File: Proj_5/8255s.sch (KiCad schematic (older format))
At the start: 18 parts, among them J1 Conn_02x15_Top_Bottom, J2 Conn_02x15_Top_Bottom, J3 Conn_02x15_Top_Bottom, U1 8255, U2 8255, U3 8255, U39 74LVC1G11, U40 74LVC1G11, U41 74AHC1G08, U42 74LVC1G11, U43 74AHC1G08, U44 74LVC1G11, U45 74AHC1G08, U46 74LVC1G11, U47 PAL16L8

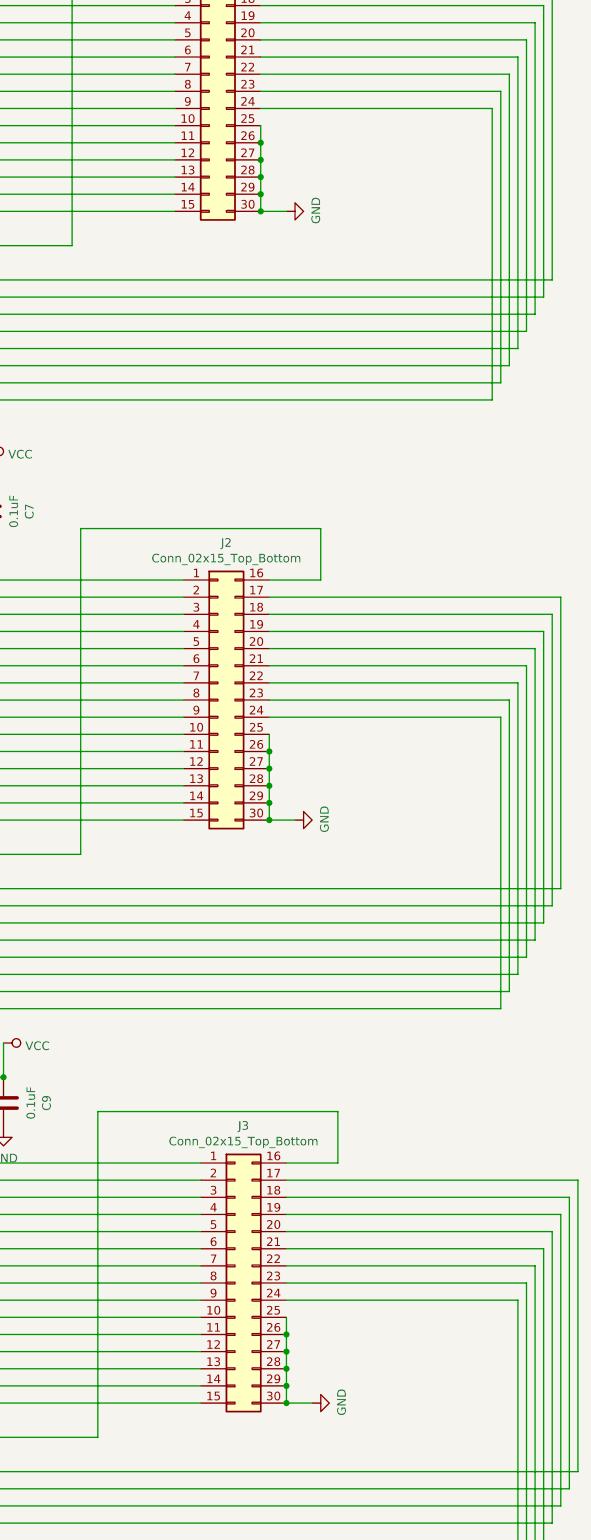
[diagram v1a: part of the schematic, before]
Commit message: Added at least 4 Footprints
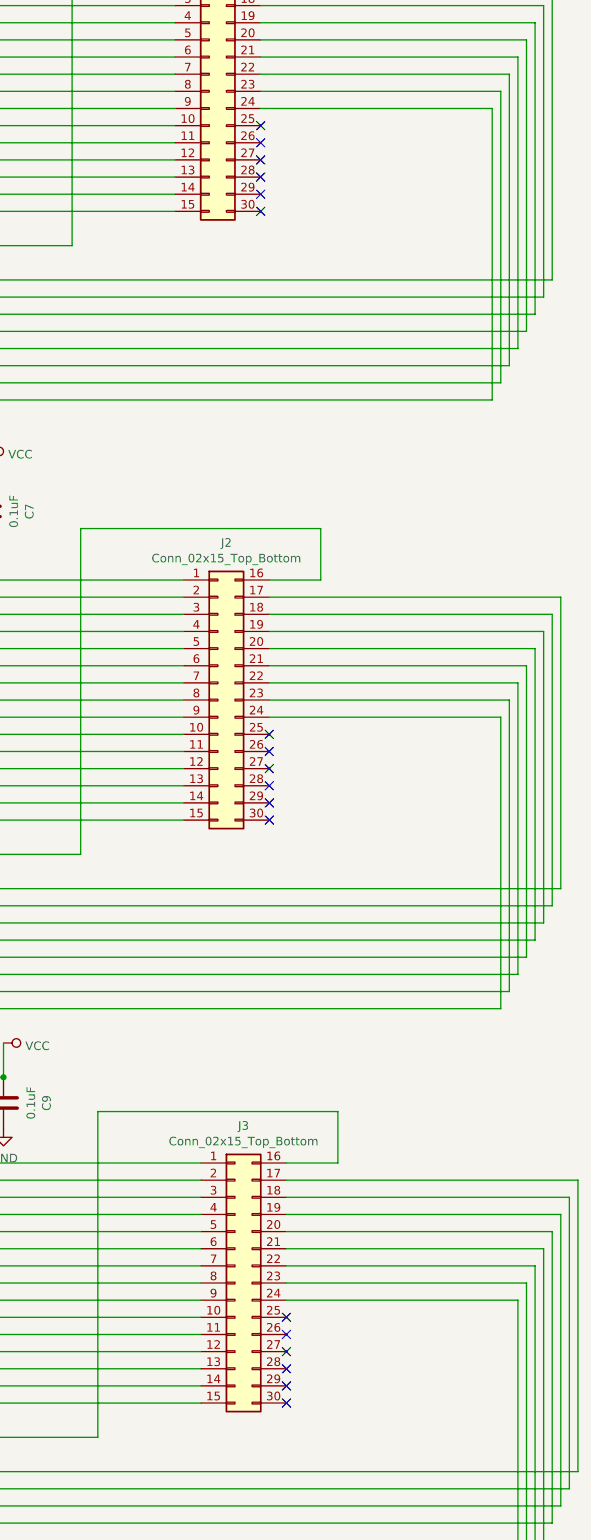
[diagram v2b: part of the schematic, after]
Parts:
- C7, C8, C9: footprint (none) -> Capacitor_Tantalum_SMD:CP_EIA-1608-08_AVX-J
- J1, J2, J3: footprint (none) -> Connector_PinHeader_1.00mm:PinHeader_2x15_P1.00mm_Vertical
- U47: footprint (none) -> Package_DIP:DIP-20_W7.62mm
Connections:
- net GND: no longer J1.25 (Pin_25), J1.26 (Pin_26), J1.27 (Pin_27), J1.28 (Pin_28), J1.29 (Pin_29), J1.30 (Pin_30), J2.25 (Pin_25), J2.26 (Pin_26), J2.27 (Pin_27), J2.28 (Pin_28), J2.29 (Pin_29), J2.30 (Pin_30), J3.25 (Pin_25), J3.26 (Pin_26), J3.27 (Pin_27), J3.28 (Pin_28), J3.29 (Pin_29), J3.30 (Pin_30)
- no-connect marks 10 -> 28
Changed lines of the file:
@@
 F 0 "U47" H 3650 5381 50  0000 C CNN
 F 1 "PAL16L8" H 3650 5290 50  0000 C CNN
-F 2 "" H 3650 4500 50  0001 C CNN
+F 2 "Package_DIP:DIP-20_W7.62mm" H 3650 4500 50  0001 C CNN
 F 3 "" H 3650 4500 50  0001 C CNN
 	1    3650 4500
@@
 F 0 "J2" H 11700 6467 50  0000 C CNN
 F 1 "Conn_02x15_Top_Bottom" H 11700 6376 50  0000 C CNN
-F 2 "" H 11650 5550 50  0001 C CNN
+F 2 "Connector_PinHeader_1.00mm:PinHeader_2x15_P1.00mm_Vertical" H 11650 5550 50  0001 C CNN
 F 3 "~" H 11650 5550 50  0001 C CNN
 	1    11650 5550
@@
 	13300 5650 11950 5650
 Wire Wire Line
-	11950 5750 11950 5850
-Connection ~ 11950 5850
-Wire Wire Line
-	11950 5850 11950 5950
-Connection ~ 11950 5950
-Wire Wire Line
-	11950 5950 11950 6050
-Connection ~ 11950 6050
-Wire Wire Line
-	11950 6050 11950 6150
-Connection ~ 11950 6150
-Wire Wire Line
-	11950 6150 11950 6250
-Wire Wire Line
-	11950 6250 12100 6250
-Connection ~ 11950 6250
-$Comp
-L power:GND #PWR?
-U 1 1 5F836F32
-P 12100 6250
-AR Path="/5EA993EC/5F836F32" Ref="#PWR?"  Part="1"
-AR Path="/5EA0416B/5F836F32" Ref="#PWR060"  Part="1"
-F 0 "#PWR060" H 12100 6000 50  0001 C CNN
-F 1 "GND" H 12105 6077 50  0000 C CNN
-F 2 "" H 12100 6250 50  0001 C CNN
-F 3 "" H 12100 6250 50  0001 C CNN
-	1    12100 6250
-	0    -1   -1   0
-$EndComp
-Wire Wire Line
 	9750 5750 9850 5750
 Wire Wire Line
@@
 F 0 "J1" H 11650 2917 50  0000 C CNN
 F 1 "Conn_02x15_Top_Bottom" H 11650 2826 50  0000 C CNN
-F 2 "" H 11600 2000 50  0001 C CNN
+F 2 "Connector_PinHeader_1.00mm:PinHeader_2x15_P1.00mm_Vertical" H 11600 2000 50  0001 C CNN
 F 3 "~" H 11600 2000 50  0001 C CNN
 	1    11600 2000
@@
 Wire Wire Line
 	13250 2100 11900 2100
-Wire Wire Line
-	11900 2200 11900 2300
-Connection ~ 11900 2300
-Wire Wire Line
-	11900 2300 11900 2400
-Connection ~ 11900 2400
-Wire Wire Line
-	11900 2400 11900 2500
-Connection ~ 11900 2500
-Wire Wire Line
-	11900 2500 11900 2600
-Connection ~ 11900 2600
-Wire Wire Line
-	11900 2600 11900 2700
-Wire Wire Line
-	11900 2700 12050 2700
-Connection ~ 11900 2700
-$Comp
-L power:GND #PWR?
-U 1 1 5F942863
-P 12050 2700
-AR Path="/5EA993EC/5F942863" Ref="#PWR?"  Part="1"
-AR Path="/5EA0416B/5F942863" Ref="#PWR059"  Part="1"
-F 0 "#PWR059" H 12050 2450 50  0001 C CNN
-F 1 "GND" H 12055 2527 50  0000 C CNN
-F 2 "" H 12050 2700 50  0001 C CNN
-F 3 "" H 12050 2700 50  0001 C CNN
-	1    12050 2700
-	0    -1   -1   0
-$EndComp
 Wire Wire Line
 	9700 2200 9800 2200
@@
 F 0 "J3" H 11800 9867 50  0000 C CNN
 F 1 "Conn_02x15_Top_Bottom" H 11800 9776 50  0000 C CNN
-F 2 "" H 11750 8950 50  0001 C CNN
+F 2 "Connector_PinHeader_1.00mm:PinHeader_2x15_P1.00mm_Vertical" H 11750 8950 50  0001 C CNN
 F 3 "~" H 11750 8950 50  0001 C CNN
 	1    11750 8950
@@
 Wire Wire Line
 	13400 9050 12050 9050
-Wire Wire Line
-	12050 9150 12050 9250
-Connection ~ 12050 9250
-Wire Wire Line
-	12050 9250 12050 9350
-Connection ~ 12050 9350
-Wire Wire Line
-	12050 9350 12050 9450
-Connection ~ 12050 9450
-Wire Wire Line
-	12050 9450 12050 9550
-Connection ~ 12050 9550
-Wire Wire Line
-	12050 9550 12050 9650
-Wire Wire Line
-	12050 9650 12200 9650
-Connection ~ 12050 9650
-$Comp
-L power:GND #PWR?
-U 1 1 5F955658
-P 12200 9650
-AR Path="/5EA993EC/5F955658" Ref="#PWR?"  Part="1"
-AR Path="/5EA0416B/5F955658" Ref="#PWR061"  Part="1"
-F 0 "#PWR061" H 12200 9400 50  0001 C CNN
-F 1 "GND" H 12205 9477 50  0000 C CNN
-F 2 "" H 12200 9650 50  0001 C CNN
-F 3 "" H 12200 9650 50  0001 C CNN
-	1    12200 9650
-	0    -1   -1   0
-$EndComp
 Wire Wire Line
 	9850 9150 9950 9150
@@
 F 0 "C9" V 10148 7900 50  0000 C CNN
 F 1 "0.1uF" V 10239 7900 50  0000 C CNN
-F 2 "" H 10438 7750 50  0001 C CNN
+F 2 "Capacitor_Tantalum_SMD:CP_EIA-1608-08_AVX-J" H 10438 7750 50  0001 C CNN
 F 3 "~" H 10400 7900 50  0001 C CNN
 	1    10400 7900
@@
 F 0 "C7" V 10048 4450 50  0000 C CNN
 F 1 "0.1uF" V 10139 4450 50  0000 C CNN
-F 2 "" H 10338 4300 50  0001 C CNN
+F 2 "Capacitor_Tantalum_SMD:CP_EIA-1608-08_AVX-J" H 10338 4300 50  0001 C CNN
 F 3 "~" H 10300 4450 50  0001 C CNN
 	1    10300 4450
@@
 F 0 "C8" V 10148 950 50  0000 C CNN
 F 1 "0.1uF" V 10239 950 50  0000 C CNN
-F 2 "" H 10438 800 50  0001 C CNN
+F 2 "Capacitor_Tantalum_SMD:CP_EIA-1608-08_AVX-J" H 10438 800 50  0001 C CNN
 F 3 "~" H 10400 950 50  0001 C CNN
 	1    10400 950
@@
 	8650 4200 9000 4200
 Connection ~ 8050 8700
+NoConn ~ 11950 5750
+NoConn ~ 11950 5850
+NoConn ~ 11950 5950
+NoConn ~ 11950 6050
+NoConn ~ 11950 6150
+NoConn ~ 11950 6250
+NoConn ~ 12050 9150
+NoConn ~ 12050 9250
+NoConn ~ 12050 9350
+NoConn ~ 12050 9450
+NoConn ~ 12050 9550
+NoConn ~ 12050 9650
+NoConn ~ 11900 2700
+NoConn ~ 11900 2600
+NoConn ~ 11900 2500
+NoConn ~ 11900 2400
+NoConn ~ 11900 2300
+NoConn ~ 11900 2200
 Wire Bus Line
 	5200 8700 8050 8700

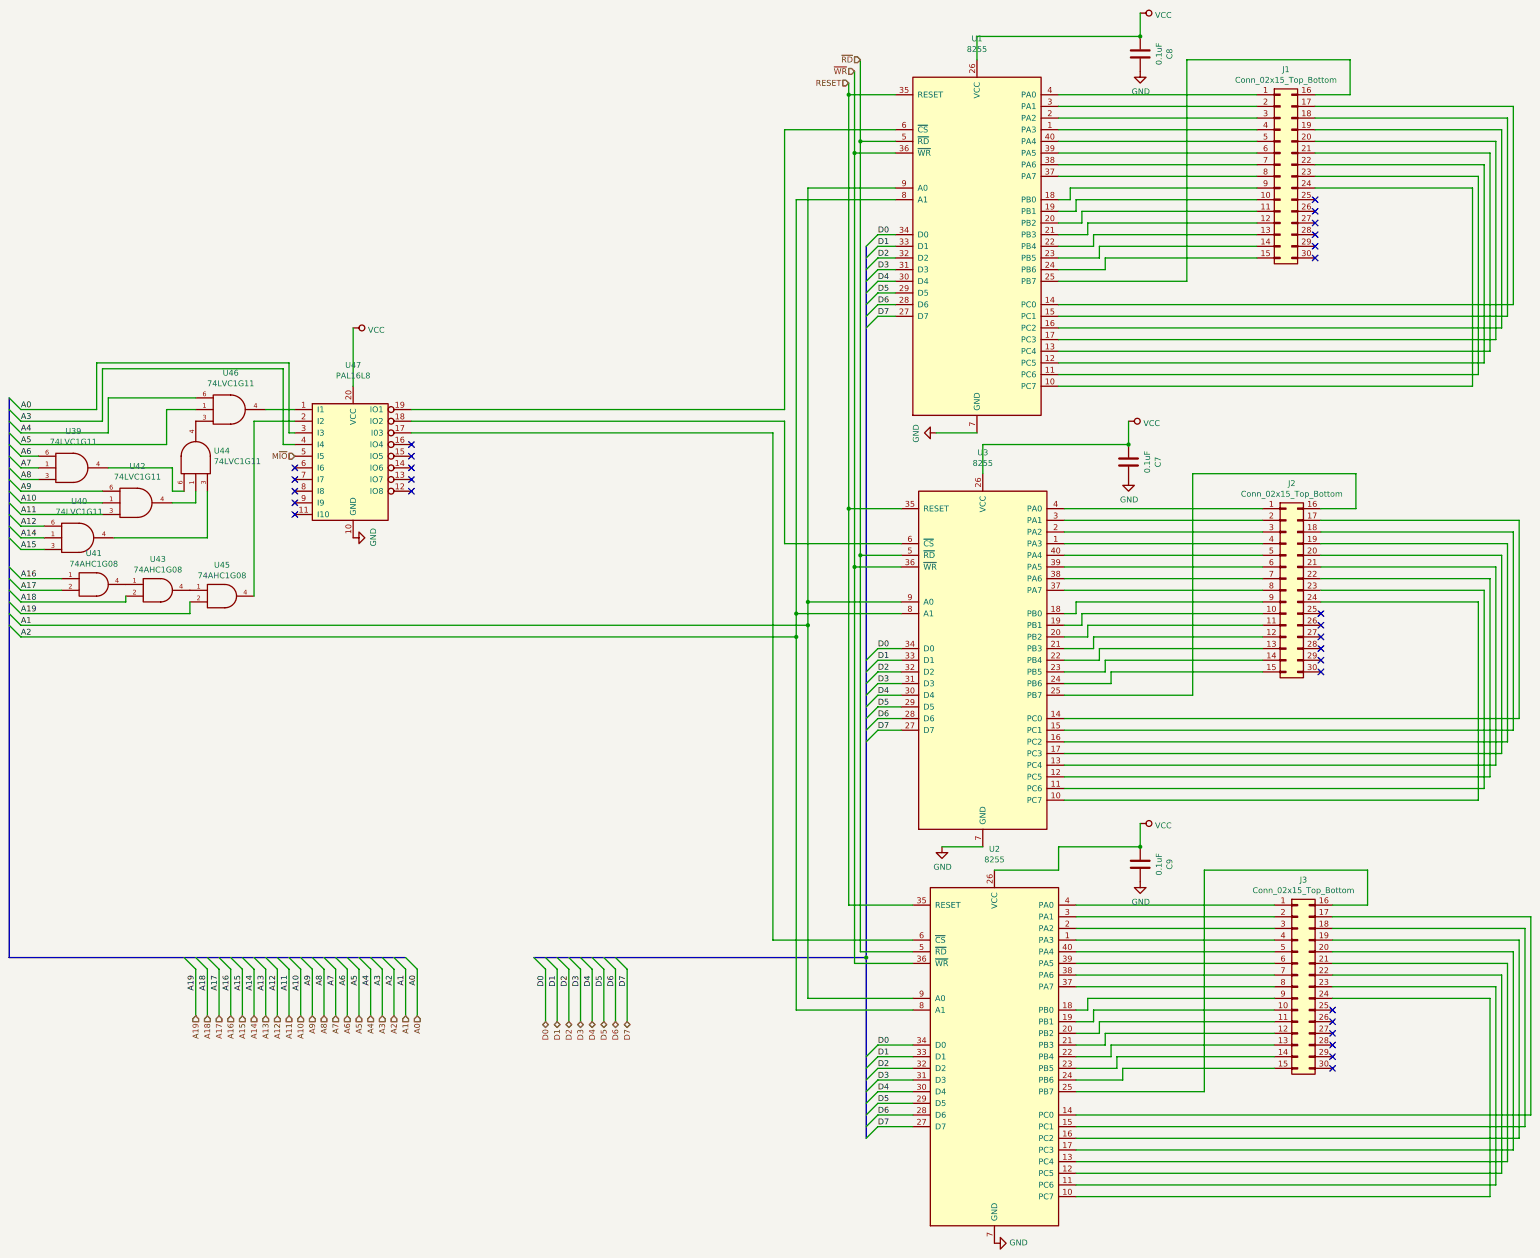
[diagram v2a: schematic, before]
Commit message: No more and gates
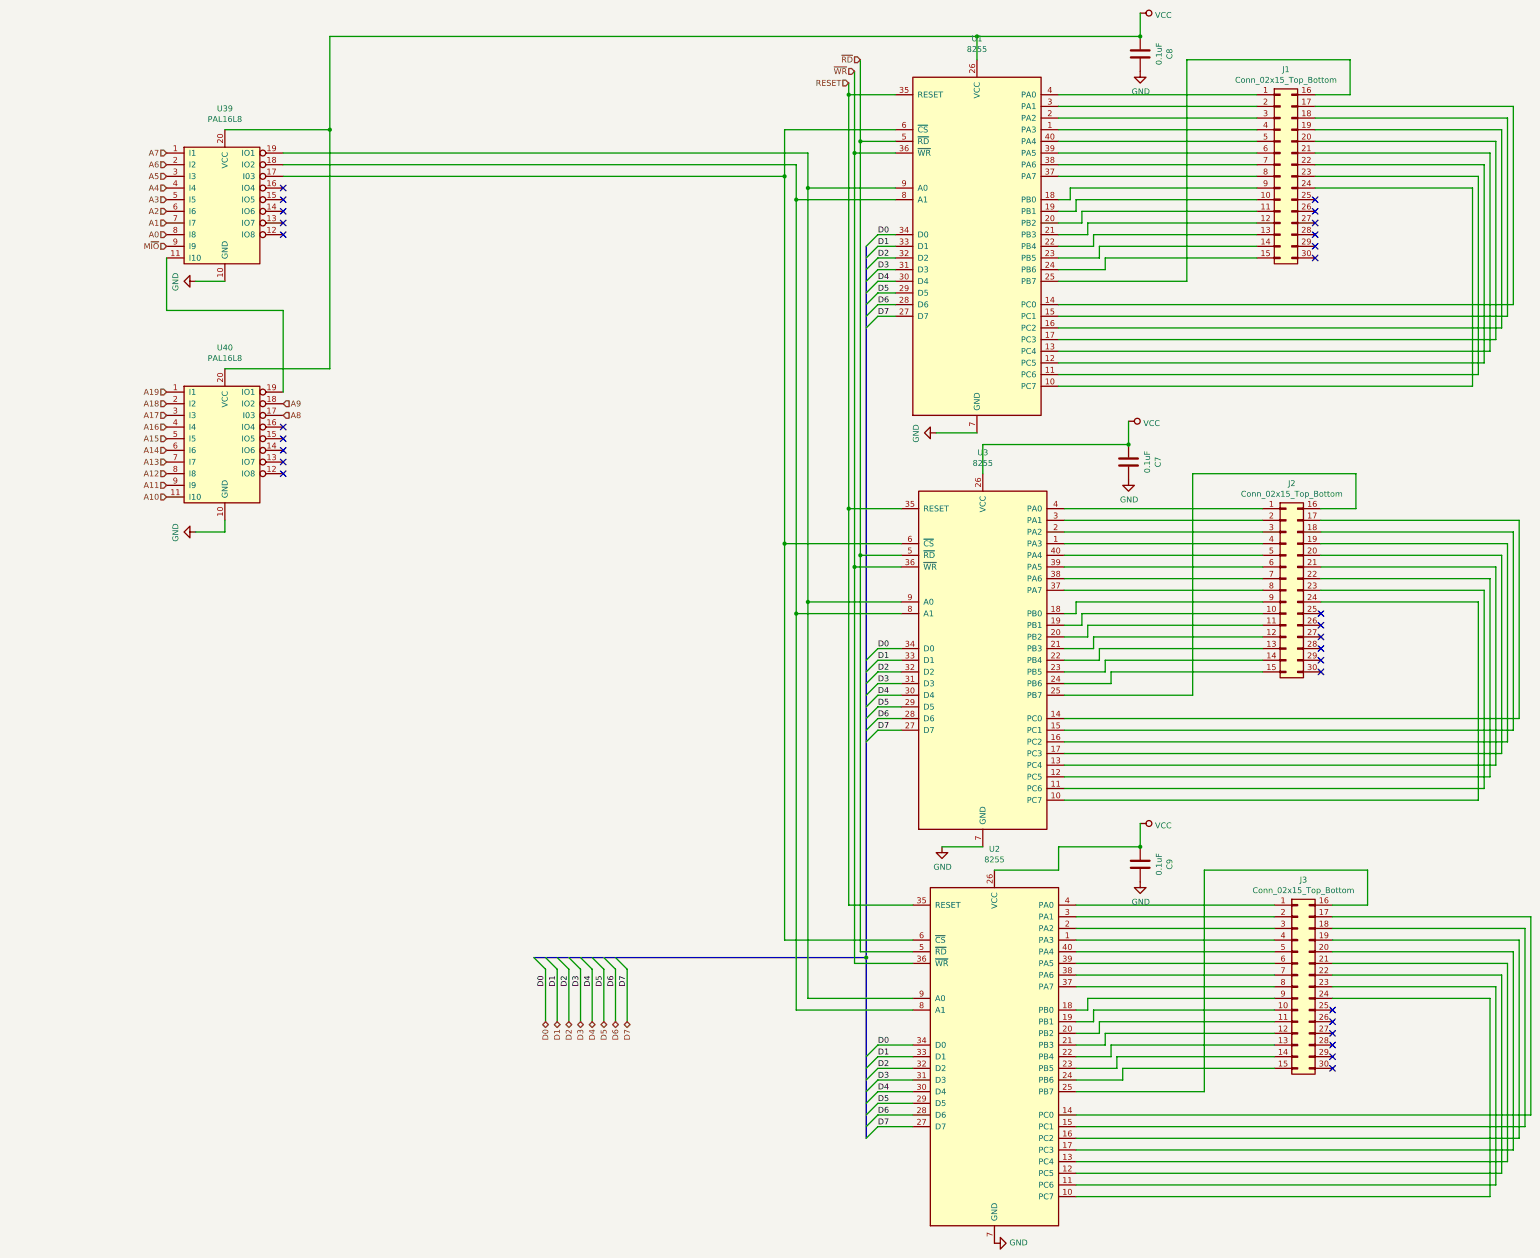
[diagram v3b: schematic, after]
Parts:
- removed U39, U40, U42, U44, U46: 74LVC1G11, symbol 74xGxx:74LVC1G11
- removed U41, U43, U45: 74AHC1G08, symbol 74xGxx:74AHC1G08
- removed U47: PAL16L8, Package_DIP:DIP-20_W7.62mm, symbol Logic_Programmable:PAL16L8
- added U39, U40: PAL16L8, Package_DIP:DIP-20_W7.62mm, symbol Logic_Programmable:PAL16L8
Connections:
- net A0: now also U39.8 (I8)
- net A1: now also U39.7 (I7); no longer U1.9 (A0), U2.9 (A0), U3.9 (A0)
- net A10: now also U40.11 (I10)
- net A11: now also U40.9 (I9)
- net A12: now also U40.8 (I8)
- net A13: now also U40.7 (I7)
- net A14: now also U40.6 (I6)
- net A15: now also U40.5 (I5)
- net A16: now also U40.4 (I4)
- net A17: now also U40.3 (I3)
- net A18: now also U40.2 (I2)
- net A19: now also U40.1 (I1)
- net A2: now also U39.6 (I6); no longer U1.8 (A1), U2.8 (A1), U3.8 (A1)
- net A3: now also U39.5 (I5)
- net A4: now also U39.4 (I4)
- net A5: now also U39.3 (I3)
- net A6: now also U39.2 (I2)
- net A7: now also U39.1 (I1)
- net A8: now also U40.17 (I03)
- net A9: now also U40.18 (IO2)
- net GND: now also U39.10 (GND), U40.10 (GND)
- net M~IO: now also U39.9 (I9)
- net VCC: now also U39.20 (VCC), U40.20 (VCC)
- net at U1.6 (~CS~): now also U2.6 (~CS~), U3.6 (~CS~), U39.17 (I03)
- new net: U1.8 (A1), U2.8 (A1), U3.8 (A1), U39.18 (IO2)
- new net: U1.9 (A0), U2.9 (A0), U3.9 (A0), U39.19 (IO1)
- new net: U39.11 (I10), U40.19 (IO1)

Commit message: Fixed 'Pad too close to Pad' Errors
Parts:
- J1, J2, J3: footprint Connector_PinHeader_1.00mm:PinHeader_2x15_P1.00mm_Vertical -> Connector_PinHeader_2.54mm:PinHeader_2x15_P2.54mm_Vertical
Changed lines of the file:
@@
 $Descr A2 23386 16535
 encoding utf-8
-Sheet 5 10
+Sheet 4 10
 Title ""
 Date ""
@@
 F 0 "J2" H 11700 6467 50  0000 C CNN
 F 1 "Conn_02x15_Top_Bottom" H 11700 6376 50  0000 C CNN
-F 2 "Connector_PinHeader_1.00mm:PinHeader_2x15_P1.00mm_Vertical" H 11650 5550 50  0001 C CNN
+F 2 "Connector_PinHeader_2.54mm:PinHeader_2x15_P2.54mm_Vertical" H 11650 5550 50  0001 C CNN
 F 3 "~" H 11650 5550 50  0001 C CNN
 	1    11650 5550
@@
 F 0 "J1" H 11650 2917 50  0000 C CNN
 F 1 "Conn_02x15_Top_Bottom" H 11650 2826 50  0000 C CNN
-F 2 "Connector_PinHeader_1.00mm:PinHeader_2x15_P1.00mm_Vertical" H 11600 2000 50  0001 C CNN
+F 2 "Connector_PinHeader_2.54mm:PinHeader_2x15_P2.54mm_Vertical" H 11600 2000 50  0001 C CNN
 F 3 "~" H 11600 2000 50  0001 C CNN
 	1    11600 2000
@@
 F 0 "J3" H 11800 9867 50  0000 C CNN
 F 1 "Conn_02x15_Top_Bottom" H 11800 9776 50  0000 C CNN
-F 2 "Connector_PinHeader_1.00mm:PinHeader_2x15_P1.00mm_Vertical" H 11750 8950 50  0001 C CNN
+F 2 "Connector_PinHeader_2.54mm:PinHeader_2x15_P2.54mm_Vertical" H 11750 8950 50  0001 C CNN
 F 3 "~" H 11750 8950 50  0001 C CNN
 	1    11750 8950

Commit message: Oh lawd he comin
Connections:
- net at U1.6 (~CS~), U39.17 (I03): no longer U2.6 (~CS~), U3.6 (~CS~)
- net at U39.15 (IO5): now also U2.6 (~CS~)
- net at U39.16 (IO4): now also U3.6 (~CS~)
- no-connect marks 28 -> 26
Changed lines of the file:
@@
 Wire Wire Line
 	7350 2000 7350 1600
-Wire Wire Line
-	7350 2000 7350 5150
-Connection ~ 7350 2000
-Wire Wire Line
-	7350 5150 7350 8550
-Connection ~ 7350 5150
-Wire Wire Line
-	7350 8550 8450 8550
 $Comp
 L power:GND #PWR?
@@
 Wire Wire Line
 	2550 5050 2300 5050
-NoConn ~ 3050 2100
-NoConn ~ 3050 2200
 NoConn ~ 3050 2300
 NoConn ~ 3050 2400
@@
 Text HLabel 2050 2600 0    50   Input ~ 0
 M~IO
+Wire Wire Line
+	3050 2100 7350 2100
+Wire Wire Line
+	7350 2100 7350 5150
+Wire Wire Line
+	3050 2200 7250 2200
+Wire Wire Line
+	7250 2200 7250 8550
+Wire Wire Line
+	7250 8550 8450 8550
 Wire Bus Line
 	8050 8700 8050 10250
